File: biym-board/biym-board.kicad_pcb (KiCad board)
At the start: 2 copper layers, 50.8 x 34 mm, 33 parts, among them J1 HEADER_01X02_JST_ZH_SMD_VERTI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, J2 HEADER_01X03_JST_ZH_SMD_VERTI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, J3 HEADER_01X04_JST_ZH_SMD_VERTI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, J4 HEADER_01X03_JST_ZH_SMD_VERTI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, J5 HEADER_01X03_JST_ZH_SMD_VERTI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, J6 HEADER_01X03_JST_ZH_SMD_VERTI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, U1 DRV8311H, U2 AS5047P, U3 LT_SN74LVC2T45DCUT, U4 BOOST_5V_RP402N501F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

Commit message: Initial v1.0 layout
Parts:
- C1, C10, C2, C5, C7, C8, C9: value C_0.1uF_0402 -> 0.1uF
- C11, C12, C13, C14, C15, C16: value C_10uF_0603 -> 10uF
- C3, C4: value C_10uF_0402_POL -> 10uF
- C6: value C_1uF_0402_POL -> 1uF
- R1, R2, R3: value R_5.1k_0402 -> 5.1k
- moved R1 20.2 mm to (119.0, 96.8), turned to 0 degrees
- moved C2 6.35 mm to (123.5, 96.8)
- moved C1 6.35 mm to (121.0, 103.2)
- moved C3 6.35 mm to (121.0, 104.4)
- moved C4 6.35 mm to (122.2, 96.8)
- moved C5 6.35 mm to (119.0, 101.3)
- moved C7 6.35 mm to (119.0, 99.4)
- moved U1 6.35 mm to (122.2, 100.0)
- moved C6 5.72 mm to (126.0, 98.1)
- moved J4 2.00 mm to (152.0, 85.0)
- moved J5 2.00 mm to (142.0, 85.0)
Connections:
- FW1 pad 3: /ENABLE_LED_POWER -> unconnected-(FW1-Pad3)
- FW1 pad 9: unconnected-(FW1-Pad9) -> /ENABLE_LED_POWER
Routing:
- net /GND: track 0.00 -> 232.5 mm, vias 0 -> 6
- net /VDIGITAL: track 0.00 -> 120.8 mm, vias 0 -> 3
- net /VBATTERY: track 0.00 -> 76.3 mm, vias 0 -> 3
- net /VSERVO: track 0.00 -> 45.6 mm, vias 0 -> 3
- net /MOSI: track 0.00 -> 30.1 mm, vias 0 -> 2
- net /DRIVER_PWM_C: track 0.00 -> 29.9 mm
- net /VLED: track 0.00 -> 29.8 mm, vias 0 -> 2
- net /DRIVER_PWM_B: track 0.00 -> 27.2 mm
- net /~{DRIVER_FAULT}: track 0.00 -> 26.8 mm
- net /servo/TRANSLATED_SIGNAL_1: track 0.00 -> 26.7 mm, vias 0 -> 2
- net /~{DRIVER_SLEEP}: track 0.00 -> 26.1 mm
- net /DRIVER_PWM_A: track 0.00 -> 24.5 mm
- net /ENABLE_LED_POWER: track 0.00 -> 22.5 mm, vias 0 -> 2
- net /driver/MOTOR_C: track 0.00 -> 20.4 mm, vias 0 -> 2
- net /SCK: track 0.00 -> 20.0 mm
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- added copper zone on B.Cu, net /GND
- added copper zone on F.Cu, net /GND
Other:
- board text added: "0"
- board text added: "1"
- board text added: "A"
- board text added: "B"
- board text added: "C"
- board text added: "D"
- board text added: "DRIVER"
- board text added: "ENCODER"
- board text added: "G"
- board text added: "GPIO"
- board text added: "LED"
- board text added: "LED POWER"
- board text added: "POWER SWITCH"
- board text added: "S"
- board text added: "SERVO 0"
- board text added: "SERVO 1"
- board text added: "SERVO POWER"
- board text added: "V"
- board text added: "biym-board v1.0 11/22 peter@polidoro.io https://github.com/biym/biym-board"

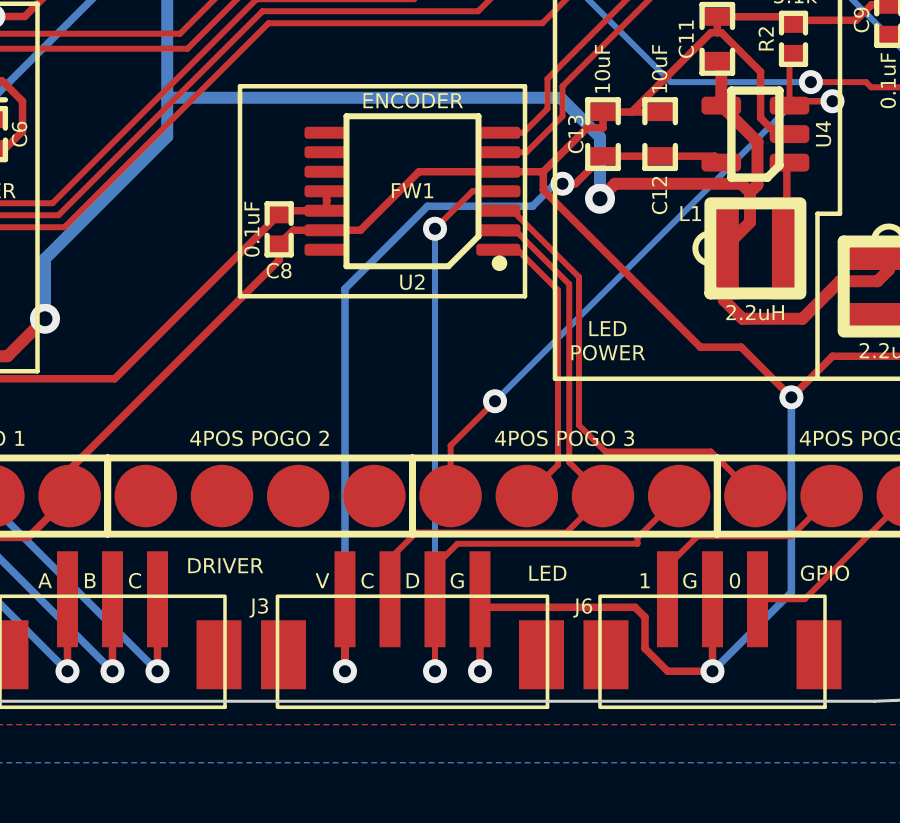
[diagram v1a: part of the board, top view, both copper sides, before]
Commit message: Moved some traces away from the encoder
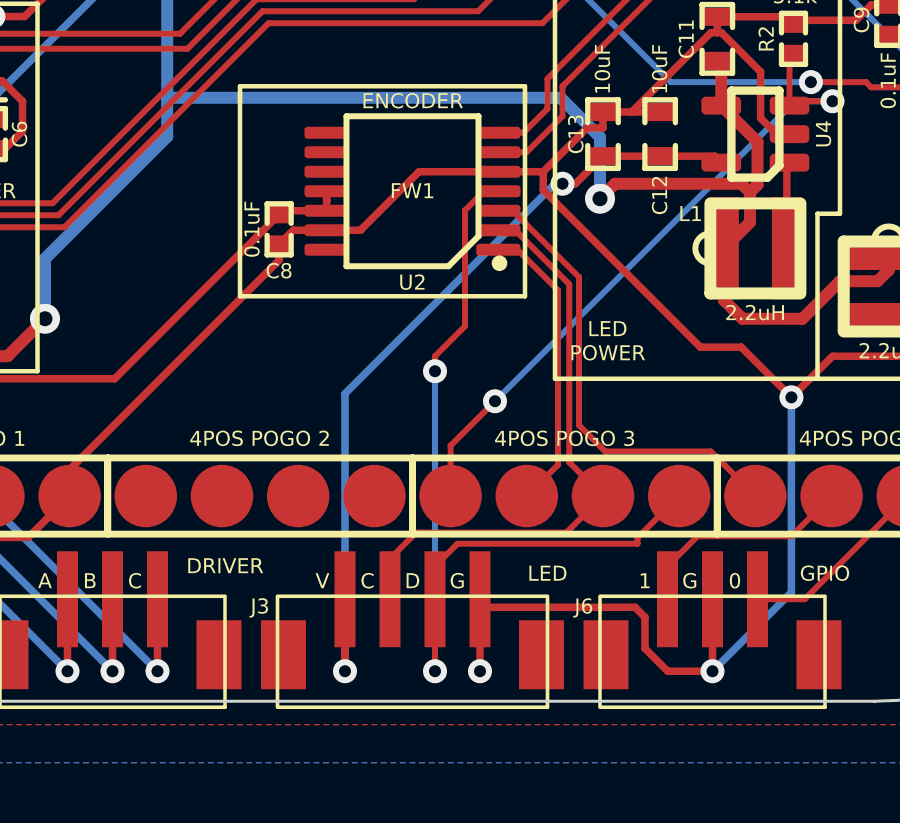
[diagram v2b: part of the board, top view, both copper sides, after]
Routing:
- net /VLED: track 29.8 -> 27.7 mm
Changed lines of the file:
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@@
   (segment (start 147.5 111.75) (end 147.5 111.55) (width 0.2) (layer "F.Cu") (net 9))
   (segment (start 147.5 111.55) (end 148.89 110.16) (width 0.2) (layer "F.Cu") (net 9))
-  (segment (start 140.75 101.25) (end 142 100) (width 0.2) (layer "F.Cu") (net 9))
   (segment (start 140.75 113.6) (end 140.75 116) (width 0.2) (layer "F.Cu") (net 9))
   (segment (start 140.75 112.5) (end 141.5 111.75) (width 0.2) (layer "F.Cu") (net 9))
+  (segment (start 141.75 100.636091) (end 142.386091 100) (width 0.2) (layer "F.Cu") (net 9))
   (segment (start 141.5 111.75) (end 147.5 111.75) (width 0.2) (layer "F.Cu") (net 9))
-  (segment (start 142.862 100) (end 142.8625 100) (width 0.2) (layer "F.Cu") (net 9))
+  (segment (start 140.75 105.5) (end 141.75 104.5) (width 0.2) (layer "F.Cu") (net 9))
+  (segment (start 140.75 106) (end 140.75 105.5) (width 0.2) (layer "F.Cu") (net 9))
+  (segment (start 142.386091 100) (end 142.8625 100) (width 0.2) (layer "F.Cu") (net 9))
   (segment (start 140.75 113.6) (end 140.75 112.5) (width 0.2) (layer "F.Cu") (net 9))
-  (segment (start 142 100) (end 142.862 100) (width 0.2) (layer "F.Cu") (net 9))
+  (segment (start 141.75 104.5) (end 141.75 100.636091) (width 0.2) (layer "F.Cu") (net 9))
   (via (at 140.75 116) (size 0.8) (drill 0.4) (layers "F.Cu" "B.Cu") (net 9))
-  (via (at 140.75 101.25) (size 0.8) (drill 0.4) (layers "F.Cu" "B.Cu") (net 9))
-  (segment (start 140.75 116) (end 140.75 101.25) (width 0.2) (layer "B.Cu") (net 9))
+  (via (at 140.75 106) (size 0.8) (drill 0.4) (layers "F.Cu" "B.Cu") (net 9))
+  (segment (start 140.75 116) (end 140.75 106) (width 0.2) (layer "B.Cu") (net 9))
   (segment (start 143.338909 100.65) (end 145.55 102.861091) (width 0.2) (layer "F.Cu") (net 10))
   (segment (start 142.862 100.65) (end 142.8625 100.65) (width 0.2) (layer "F.Cu") (net 10))
@@
   (via (at 145 99.75) (size 0.8) (drill 0.4) (layers "F.Cu" "B.Cu") (net 12))
   (via (at 137.75 116) (size 0.8) (drill 0.4) (layers "F.Cu" "B.Cu") (net 12))
+  (segment (start 137.75 116) (end 137.75 106.75) (width 0.25) (layer "B.Cu") (net 12))
+  (segment (start 137.75 106.75) (end 144.75 99.75) (width 0.25) (layer "B.Cu") (net 12))
   (segment (start 144.75 99.75) (end 145 99.75) (width 0.25) (layer "B.Cu") (net 12))
-  (segment (start 144 100.5) (end 144.75 99.75) (width 0.25) (layer "B.Cu") (net 12))
-  (segment (start 137.75 103.25) (end 140.5 100.5) (width 0.25) (layer "B.Cu") (net 12))
-  (segment (start 137.75 116) (end 137.75 103.25) (width 0.25) (layer "B.Cu") (net 12))
-  (segment (start 140.5 100.5) (end 144 100.5) (width 0.25) (layer "B.Cu") (net 12))
   (segment (start 138.73 89.84) (end 138.73 92.27) (width 0.2) (layer "F.Cu") (net 13))
   (segment (start 138.25 92.75) (end 134.25 92.75) (width 0.2) (layer "F.Cu") (net 13))

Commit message: Completed v1.1 layout
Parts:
- added P1: POGO_01X16_0.1IN_1_SMD, Janelia:POGO_01x16_0.1in_SMD, F.Cu at (140.0, 110.2)
- added P2: POGO_01X12_0.1IN_1_SMD, Janelia:POGO_01x12_0.1in_SMD, F.Cu at (145.1, 89.8)
- FW1: value FEATHERWING_nRF52_POGO_PINS -> FEATHERWING_nRF52; footprint Janelia:FEATHERWING_POGO_PINS -> Janelia:FEATHERWING
- moved C6 0.67 mm to (125.5, 98.5)
- moved C5 0.07 mm to (119.0, 101.2)
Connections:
- net /power/boost_led/LX renamed /power/boost-led/LX
- net /power/boost_servo/LX renamed /power/boost-servo/LX
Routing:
- net /VDIGITAL: track 120.8 -> 88.6 mm, vias 3 -> 4
- net /GND: track 232.5 -> 218.1 mm, vias 6 -> 0
- net /VSERVO: track 45.6 -> 39.4 mm
- net /MOSI: track 29.9 -> 24.0 mm
- net /~{DRIVER_FAULT}: track 26.8 -> 30.2 mm
- net /servo/TRANSLATED_SIGNAL_1: track 26.7 -> 23.7 mm
- net /servo/TRANSLATED_SIGNAL_0: track 19.2 -> 16.6 mm, vias 3 -> 2
- net /VLED: track 27.7 -> 25.7 mm
- net /~{ENCODER_CS}: track 9.84 -> 11.8 mm
- net /ENABLE_LED_POWER: track 22.5 -> 21.0 mm
- net /DRIVER_PWM_A: track 24.5 -> 25.9 mm
- net /~{DRIVER_SLEEP}: track 26.1 -> 26.8 mm, vias 0 -> 2
- net /ENCODER_B: track 15.4 -> 15.9 mm
- net /GPIO_0: track 6.43 -> 6.98 mm
- net /SCK: track 20.0 -> 20.5 mm
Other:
- board text added: "biym-board v1.1 11/22 peter@polidoro.io https://github.com/biym/biym-board"
- board text removed: "biym-board v1.0 11/22 peter@polidoro.io https://github.com/biym/biym-board"

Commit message: Adjust after circuithub import test
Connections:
- net /featherwing_nrf52_pogo/GPIO/14/A0-HS renamed /featherwing-nrf52-pogo/GPIO/14/A0-HS
- net /featherwing_nrf52_pogo/GPIO/15/A1-HS renamed /featherwing-nrf52-pogo/GPIO/15/A1-HS
- net /featherwing_nrf52_pogo/GPIO/16/A2-LS renamed /featherwing-nrf52-pogo/GPIO/16/A2-LS
- net /featherwing_nrf52_pogo/GPIO/17/A3-LS renamed /featherwing-nrf52-pogo/GPIO/17/A3-LS
- net /featherwing_nrf52_pogo/GPIO/21/AREF/A7-LS renamed /featherwing-nrf52-pogo/GPIO/21/AREF/A7-LS
- net /featherwing_nrf52_pogo/VUSB renamed /featherwing-nrf52-pogo/VUSB
- net /featherwing_nrf52_pogo/~{RESET} renamed /featherwing-nrf52-pogo/~{RESET}
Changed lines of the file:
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@@
   (net 42 "unconnected-(U2-Pad10)")
   (net 43 "unconnected-(U2-Pad14)")
-  (net 44 "/featherwing_nrf52_pogo/~{RESET}")
-  (net 45 "/featherwing_nrf52_pogo/GPIO{slash}21{slash}AREF{slash}A7-LS")
-  (net 46 "/featherwing_nrf52_pogo/GPIO{slash}14{slash}A0-HS")
-  (net 47 "/featherwing_nrf52_pogo/GPIO{slash}15{slash}A1-HS")
-  (net 48 "/featherwing_nrf52_pogo/GPIO{slash}16{slash}A2-LS")
-  (net 49 "/featherwing_nrf52_pogo/GPIO{slash}17{slash}A3-LS")
-  (net 50 "/featherwing_nrf52_pogo/VUSB")
+  (net 44 "/featherwing-nrf52-pogo/~{RESET}")
+  (net 45 "/featherwing-nrf52-pogo/GPIO{slash}21{slash}AREF{slash}A7-LS")
+  (net 46 "/featherwing-nrf52-pogo/GPIO{slash}14{slash}A0-HS")
+  (net 47 "/featherwing-nrf52-pogo/GPIO{slash}15{slash}A1-HS")
+  (net 48 "/featherwing-nrf52-pogo/GPIO{slash}16{slash}A2-LS")
+  (net 49 "/featherwing-nrf52-pogo/GPIO{slash}17{slash}A3-LS")
+  (net 50 "/featherwing-nrf52-pogo/VUSB")
   (footprint "Janelia:SM0603" (layer "F.Cu")
     (at 146.35 98.095 180)
@@
   (footprint "Janelia:FEATHERWING" locked (layer "F.Cu")
     (at 140 100)
-    (property "Sheetfile" "featherwing_nrf52_pogo.kicad_sch")
-    (property "Sheetname" "featherwing_nrf52_pogo")
+    (property "Sheetfile" "featherwing-nrf52-pogo.kicad_sch")
+    (property "Sheetname" "featherwing-nrf52-pogo")
     (fp_text reference "FW1" (at 0 0) (layer "F.Fab")
       (effects (font (size 1.27 1.27) (thickness 0.3175)))
@@
     (property "Manufacturer" "Mill-Max Manufacturing Corp.")
     (property "Manufacturer Part Number" "811-22-012-30-001101")
-    (property "Sheetfile" "featherwing_nrf52_pogo.kicad_sch")
-    (property "Sheetname" "featherwing_nrf52_pogo")
+    (property "Sheetfile" "featherwing-nrf52-pogo.kicad_sch")
+    (property "Sheetname" "featherwing-nrf52-pogo")
     (property "Vendor" "Digi-Key")
     (property "Vendor Part Number" "ED8111-12-ND")
@@
       (net 12 "/~{DRIVER_FAULT}") (pinfunction "P9") (pintype "passive"))
     (pad "10" smd circle (at 8.89 0 180) (size 2.0828 2.0828) (layers "F.Cu" "F.Paste" "F.Mask")
-      (net 50 "/featherwing_nrf52_pogo/VUSB") (pinfunction "P10") (pintype "passive"))
+      (net 50 "/featherwing-nrf52-pogo/VUSB") (pinfunction "P10") (pintype "passive"))
     (pad "11" smd circle (at 11.43 0 180) (size 2.0828 2.0828) (layers "F.Cu" "F.Paste" "F.Mask")
       (net 17 "/~{DISABLE_ALL_POWER}") (pinfunction "P11") (pintype "passive"))
@@
     (property "Manufacturer" "Mill-Max Manufacturing Corp.")
     (property "Manufacturer Part Number" "811-22-016-30-001101")
-    (property "Sheetfile" "featherwing_nrf52_pogo.kicad_sch")
-    (property "Sheetname" "featherwing_nrf52_pogo")
+    (property "Sheetfile" "featherwing-nrf52-pogo.kicad_sch")
+    (property "Sheetname" "featherwing-nrf52-pogo")
     (property "Vendor" "Digi-Key")
     (property "Vendor Part Number" "ED8111-16-ND")
@@
     (fp_rect (start -20.32 -1.27) (end 20.32 1.27) (layer "F.SilkS") (width 0.2) (fill none))
     (pad "1" smd rect (at -19.05 0) (size 2.0828 2.0828) (layers "F.Cu" "F.Paste" "F.Mask")
-      (net 44 "/featherwing_nrf52_pogo/~{RESET}") (pinfunction "P1") (pintype "passive"))
+      (net 44 "/featherwing-nrf52-pogo/~{RESET}") (pinfunction "P1") (pintype "passive"))
     (pad "2" smd circle (at -16.51 0) (size 2.0828 2.0828) (layers "F.Cu" "F.Paste" "F.Mask")
       (net 1 "/VDIGITAL") (pinfunction "P2") (pintype "passive"))
     (pad "3" smd circle (at -13.97 0) (size 2.0828 2.0828) (layers "F.Cu" "F.Paste" "F.Mask")
-      (net 45 "/featherwing_nrf52_pogo/GPIO{slash}21{slash}AREF{slash}A7-LS") (pinfunction "P3") (pintype "passive"))
+      (net 45 "/featherwing-nrf52-pogo/GPIO{slash}21{slash}AREF{slash}A7-LS") (pinfunction "P3") (pintype "passive"))
     (pad "4" smd circle (at -11.43 0) (size 2.0828 2.0828) (layers "F.Cu" "F.Paste" "F.Mask")
       (net 2 "/GND") (pinfunction "P4") (pintype "passive"))
     (pad "5" smd circle (at -8.89 0) (size 2.0828 2.0828) (layers "F.Cu" "F.Paste" "F.Mask")
-      (net 46 "/featherwing_nrf52_pogo/GPIO{slash}14{slash}A0-HS") (pinfunction "P5") (pintype "passive"))
+      (net 46 "/featherwing-nrf52-pogo/GPIO{slash}14{slash}A0-HS") (pinfunction "P5") (pintype "passive"))
     (pad "6" smd circle (at -6.35 0) (size 2.0828 2.0828) (layers "F.Cu" "F.Paste" "F.Mask")
-      (net 47 "/featherwing_nrf52_pogo/GPIO{slash}15{slash}A1-HS") (pinfunction "P6") (pintype "passive"))
+      (net 47 "/featherwing-nrf52-pogo/GPIO{slash}15{slash}A1-HS") (pinfunction "P6") (pintype "passive"))
     (pad "7" smd circle (at -3.81 0) (size 2.0828 2.0828) (layers "F.Cu" "F.Paste" "F.Mask")
-      (net 48 "/featherwing_nrf52_pogo/GPIO{slash}16{slash}A2-LS") (pinfunction "P7") (pintype "passive"))
+      (net 48 "/featherwing-nrf52-pogo/GPIO{slash}16{slash}A2-LS") (pinfunction "P7") (pintype "passive"))
     (pad "8" smd circle (at -1.27 0) (size 2.0828 2.0828) (layers "F.Cu" "F.Paste" "F.Mask")
-      (net 49 "/featherwing_nrf52_pogo/GPIO{slash}17{slash}A3-LS") (pinfunction "P8") (pintype "passive"))
+      (net 49 "/featherwing-nrf52-pogo/GPIO{slash}17{slash}A3-LS") (pinfunction "P8") (pintype "passive"))
     (pad "9" smd circle (at 1.27 0) (size 2.0828 2.0828) (layers "F.Cu" "F.Paste" "F.Mask")
       (net 18 "/ENABLE_LED_POWER") (pinfunction "P9") (pintype "passive"))
@@
     (tags "TSSOP SO")
     (property "Description" "ROTARY ENCODER MAGNETIC PROG")
-    (property "Manufacturer" "ams OSRAM")
+    (property "Manufacturer" "Osram")
     (property "Manufacturer Part Number" "AS5047P-ATSM")
     (property "Sheetfile" "encoder.kicad_sch")

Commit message: Finished v1.2
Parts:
- added FID1: FIDUCIAL_0.5mm_MASK1mm, Janelia:FIDUCIAL_0.5mm_Mask1mm, F.Cu at (120.0, 86.0)
- added FID2: FIDUCIAL_0.5mm_MASK1mm, Janelia:FIDUCIAL_0.5mm_Mask1mm, F.Cu at (160.0, 86.0)
- added FID3: FIDUCIAL_0.5mm_MASK1mm, Janelia:FIDUCIAL_0.5mm_Mask1mm, F.Cu at (160.0, 114.0)
- added FID4: FIDUCIAL_0.5mm_MASK1mm, Janelia:FIDUCIAL_0.5mm_Mask1mm, F.Cu at (120.0, 114.0)
- added P3: POGO_01X04_0.1IN_1_SMD, Janelia:POGO_01x04_0.1in_SMD, F.Cu at (145.1, 110.2)
- added P4: POGO_01X04_0.1IN_1_SMD, Janelia:POGO_01x04_0.1in_SMD, F.Cu at (155.2, 110.2)
- added P5: POGO_01X04_0.1IN_1_SMD, Janelia:POGO_01x04_0.1in_SMD, F.Cu at (155.2, 89.8)
- added P6: POGO_01X04_0.1IN_1_SMD, Janelia:POGO_01x04_0.1in_SMD, F.Cu at (145.1, 89.8)
- added P7: POGO_01X04_0.1IN_1_SMD, Janelia:POGO_01x04_0.1in_SMD, F.Cu at (134.9, 89.8)
- P1: value POGO_01X16_0.1IN_1_SMD -> POGO_01X04_0.1IN_1_SMD; footprint Janelia:POGO_01x16_0.1in_SMD -> Janelia:POGO_01x04_0.1in_SMD
- P2: value POGO_01X12_0.1IN_1_SMD -> POGO_01X04_0.1IN_1_SMD; footprint Janelia:POGO_01x12_0.1in_SMD -> Janelia:POGO_01x04_0.1in_SMD
- moved P2 22.7 mm to (134.9, 110.2), turned to 0 degrees
- moved P1 15.2 mm to (124.8, 110.2)
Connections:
- P2 pad 1: /SERVO_SIGNAL_0 -> /featherwing-nrf52-pogo/GPIO/14/A0-HS
- P2 pad 2: /SERVO_SIGNAL_1 -> /featherwing-nrf52-pogo/GPIO/15/A1-HS
- P2 pad 3: /ENCODER_B -> /featherwing-nrf52-pogo/GPIO/16/A2-LS
- P2 pad 4: /ENCODER_A -> /featherwing-nrf52-pogo/GPIO/17/A3-LS
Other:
- board text added: "biym-board v1.2 11/22 peter@polidoro.io https://github.com/biym/biym-board"
- board text removed: "biym-board v1.1 11/22 peter@polidoro.io https://github.com/biym/biym-board"
